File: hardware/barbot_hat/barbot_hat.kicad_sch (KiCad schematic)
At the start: 11 parts, among them J1 GPIO, J2 Conn_01x02, J3 Conn_01x02, J4 Conn_01x02, J5 Conn_01x02, U1 CAT24C256

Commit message: Work on layout
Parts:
- removed J2, J3, J4, J5: Conn_01x02, Connector_PinHeader_2.54mm:PinHeader_1x02_P2.54mm_Horizontal, symbol Connector_Generic:Conn_01x02
- added A2: Pololu_Breakout_A4988, Module:Pololu_Breakout-16_15.2x20.3mm, symbol Driver_Motor:Pololu_Breakout_A4988
- added C2: C_Polarized, Capacitor_THT:CP_Radial_D10.0mm_P5.00mm, symbol Device:C_Polarized
- added C3: C, Capacitor_SMD:C_0805_2012Metric_Pad1.18x1.45mm_HandSolder, symbol Device:C
- added D1, D2: WS2812B, LED_SMD:LED_WS2812B_PLCC4_5.0x5.0mm_P3.2mm, symbol LED:WS2812B
- added D3: D, Diode_THT:D_DO-27_P5.08mm_Vertical_AnodeUp, symbol Device:D
- added J7: Conn_01x03, Connector_PinHeader_2.54mm:PinHeader_1x03_P2.54mm_Horizontal, symbol Connector_Generic:Conn_01x03
- added J8: Conn_01x04, Connector_PinHeader_2.54mm:PinHeader_1x04_P2.54mm_Horizontal, symbol Connector_Generic:Conn_01x04
- added J9: Screw_Terminal_01x02, TerminalBlock:TerminalBlock_bornier-2_P5.08mm, symbol Connector:Screw_Terminal_01x02
- added U8: SN74LV1T34DBV, Package_TO_SOT_SMD:SOT-23-5, symbol Logic_LevelTranslator:SN74LV1T34DBV
- C1: footprint (none) -> Capacitor_SMD:C_0603_1608Metric_Pad1.08x0.95mm_HandSolder; now not fitted; now left out of the parts list
- JP1: footprint (none) -> Jumper:SolderJumper-2_P1.3mm_Open_TrianglePad1.0x1.5mm; now not fitted; now left out of the parts list
- R1, R2: footprint (none) -> Resistor_SMD:R_0603_1608Metric_Pad0.98x0.95mm_HandSolder; now not fitted; now left out of the parts list
- U1: footprint (none) -> Package_SO:SOIC-8_3.9x4.9mm_P1.27mm; now not fitted; now left out of the parts list
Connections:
- net +3V3: now also A2.10 (MS1), A2.11 (MS2), A2.2 (VDD)
- net +5V: now also C3.1, D1.1 (VDD), D2.1 (VDD), D3.2 (A), J7.1 (Pin_1), U8.5 (VCC)
- net GND: now also A2.1 (GND), A2.12 (MS3), A2.7 (GND), C2.2, C3.2, D1.3 (VSS), D2.3 (VSS), J7.3 (Pin_3), J9.1 (Pin_1), U8.3 (GND)
- net at U2.14 (5V): now also D3.1 (K)
- net PUMP_CTRL3: now reaches U2.2 (GPIO3)
- net PUMP_CTRL2: now reaches U2.3 (GPIO4)
- net PUMP_CTRL1: now reaches U2.4 (GPIO5)
- net PUMP_CTRL0: now reaches U2.5 (GPIO6)
- net MOTOR_Z: now reaches U2.6 (GPIO7)
- net MOTOR_X_DIR: now reaches U2.7 (GPIO21)
- net MOTOR_X_DIR: now also A2.16 (DIR)
- net MOTOR_X_STEP: now reaches U2.8 (GPIO20)
- net MOTOR_X_STEP: now also A2.15 (STEP)
- net GPIO22 renamed GPIO22 / NEOPIXEL_IN
- net GPIO22 / NEOPIXEL_IN: now also U8.2 (A)
- new net: A2.13 (~{RESET}), A2.14 (~{SLEEP})
- new net: A2.3 (1B), J8.4 (Pin_4)
- new net: A2.4 (1A), J8.3 (Pin_3)
- new net: A2.5 (2A), J8.2 (Pin_2)
- new net: A2.6 (2B), J8.1 (Pin_1)
- new net: D1.2 (DOUT), D2.4 (DIN)
- new net: D1.4 (DIN), U8.4 (Y)
- new net +12V: A2.8 (VMOT), C2.1, J9.2 (Pin_2)
- new net NEOPIXEL_OUT: D2.2 (DOUT), J7.2 (Pin_2)
- no-connect marks 10 -> 15
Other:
- added sheet Pump Motor0 (pump_motor.kicad_sch)
- added sheet Pump Motor1 (pump_motor.kicad_sch)
- added sheet Pump Motor2 (pump_motor.kicad_sch)
- added sheet Pump Motor3 (pump_motor.kicad_sch)
- added sheet Pump Motor4 (pump_motor.kicad_sch)
- moved on the sheet: U2

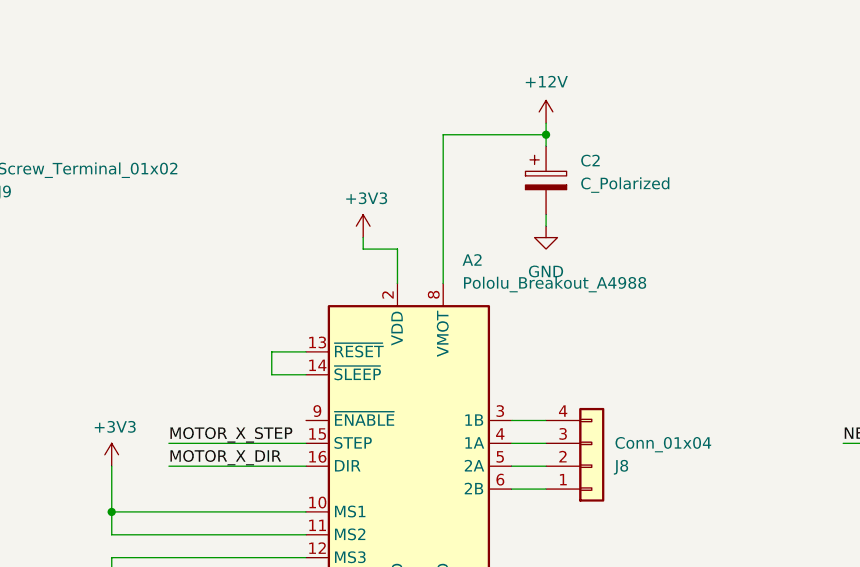
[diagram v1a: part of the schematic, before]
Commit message: Add stepper ref image to schematic
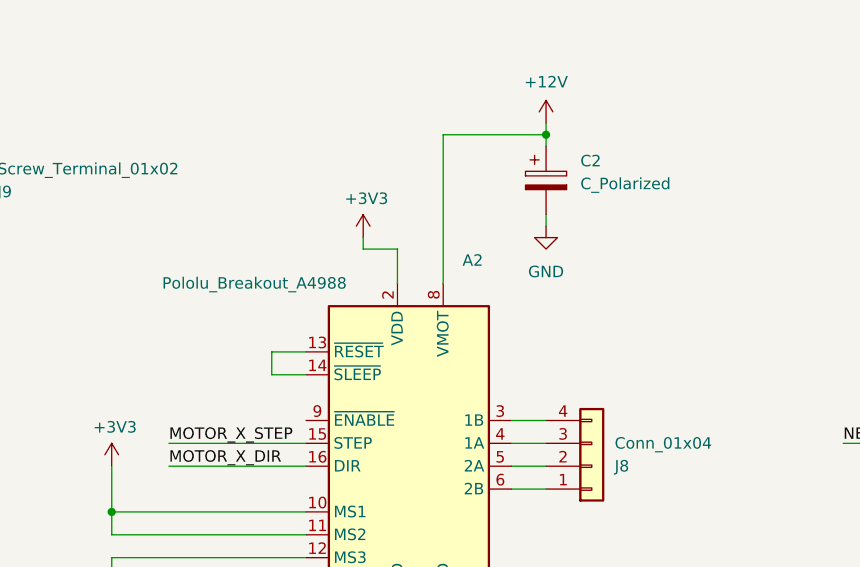
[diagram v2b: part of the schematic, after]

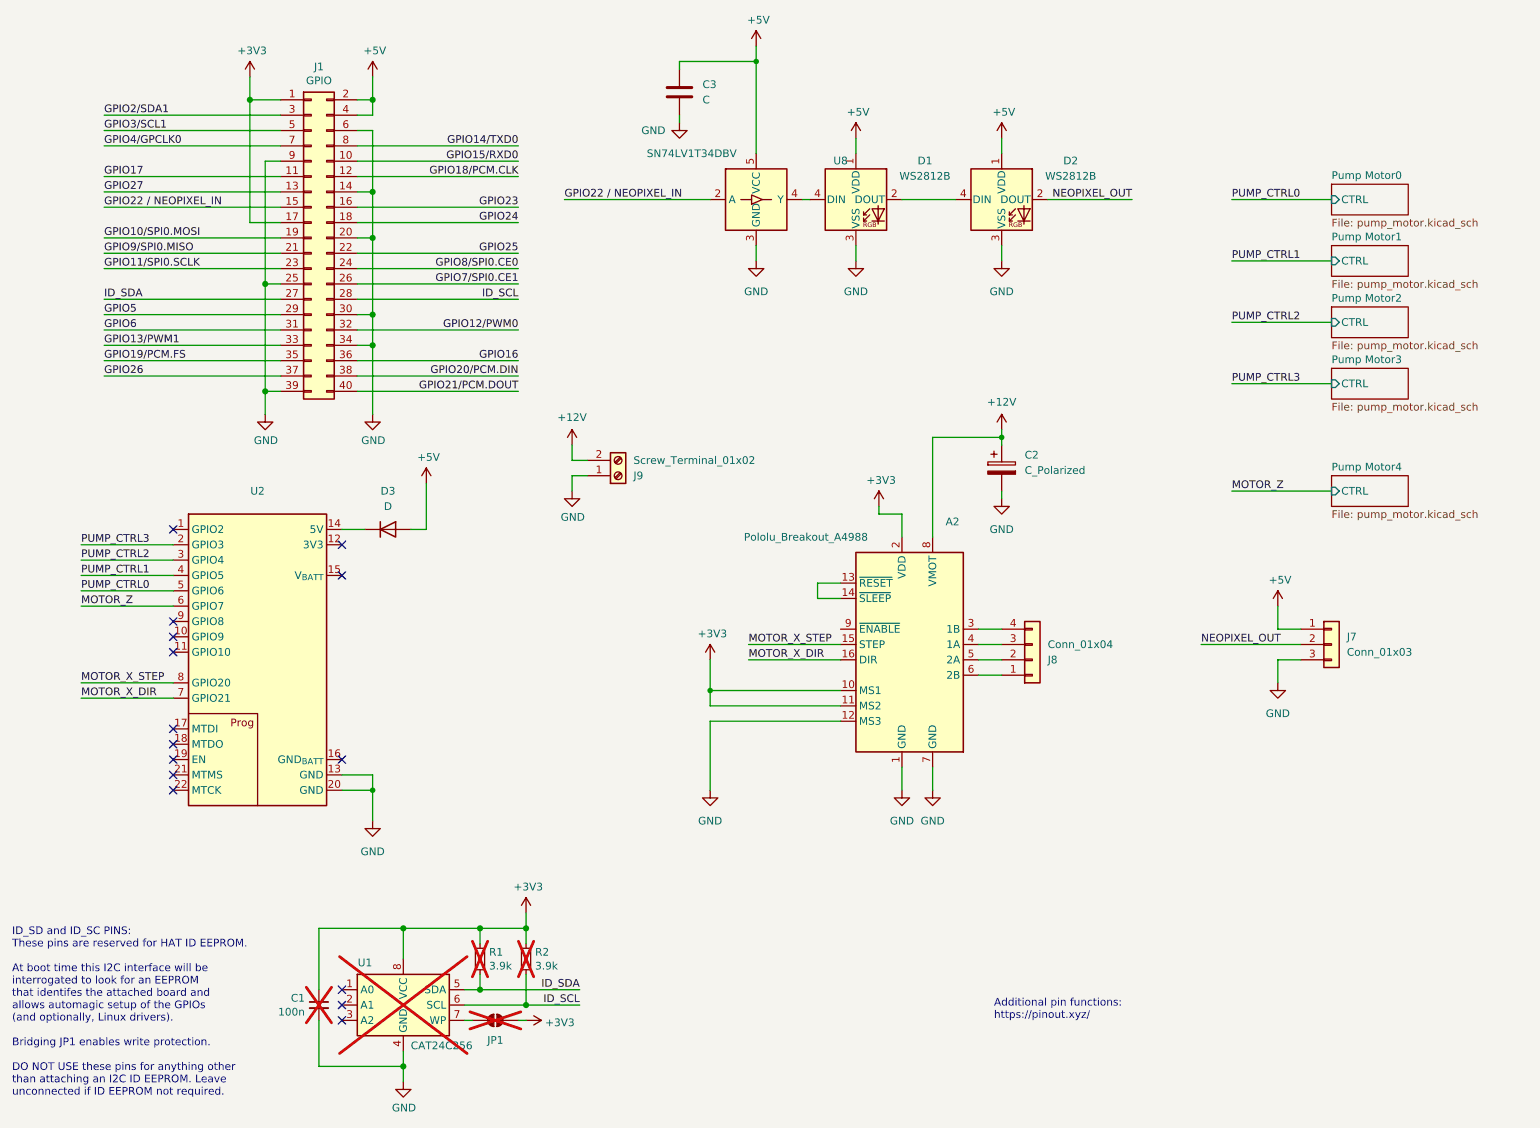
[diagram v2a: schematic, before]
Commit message: Change power delivery, update logo
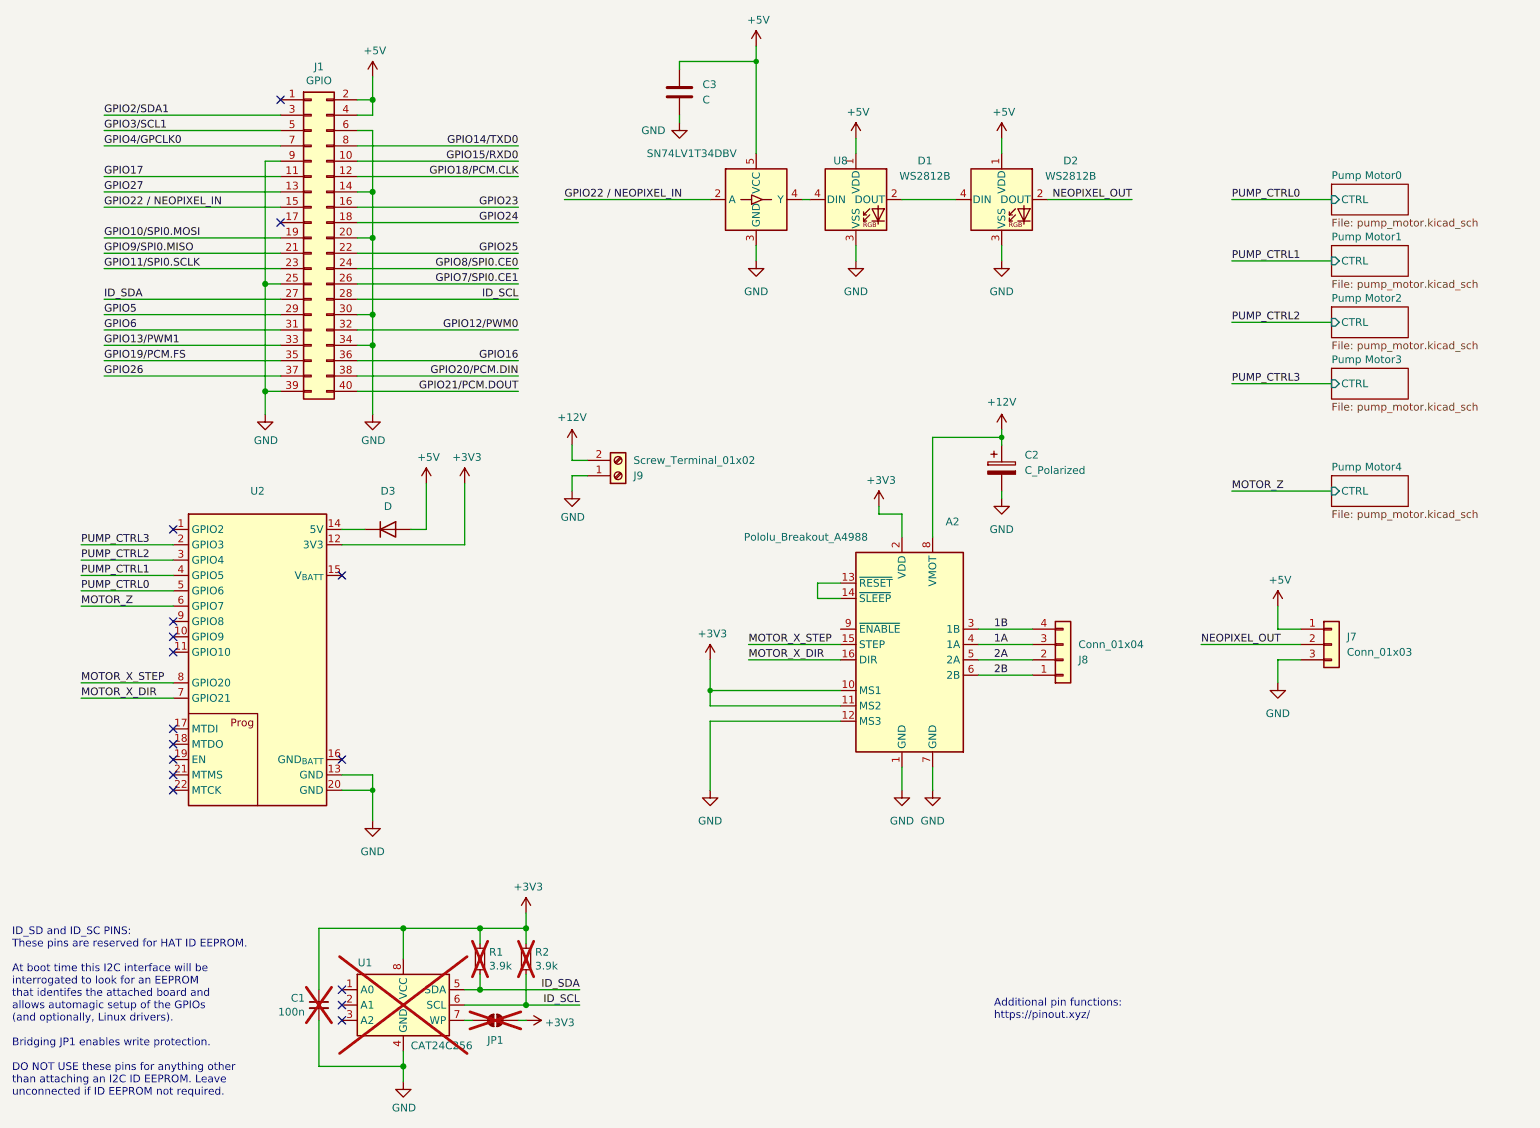
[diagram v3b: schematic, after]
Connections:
- net +3V3: now also U2.12 (3V3); no longer J1.1 (Pin_1), J1.17 (Pin_17)
- net 1B: now reaches A2.3 (1B), J8.4 (Pin_4)
- net 1A: now reaches A2.4 (1A), J8.3 (Pin_3)
- net 2A: now reaches A2.5 (2A), J8.2 (Pin_2)
- net 2B: now reaches A2.6 (2B), J8.1 (Pin_1)
- no-connect marks 15 -> 16
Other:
- moved on the sheet: J8
